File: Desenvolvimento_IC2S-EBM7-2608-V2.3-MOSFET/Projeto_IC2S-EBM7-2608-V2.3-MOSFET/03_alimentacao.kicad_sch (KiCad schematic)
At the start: 29 parts, among them T10 TP_DGND, T4 TP_+5V_REG, T5 TP_+3.3V_ANA, T6 TP_+3.3V_DIG, U14 TL431B, U3 R-78HB5.0-0.5L, U4 SPX3819M5-L-3-3/TR, U8 MCP1824ST-3302E/DB

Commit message: Revisao da reuniao 28-09: ramo unico de 24 V, 100 nF a 50 V, um so MPN de 1 uF
- Saem F2, o diodo e o condensador do ramo +24V_ADC; F1 + diodo alimentam o
  R-78HB e o +24V_ADC. +24V_REG deixa de existir (esquematico, PCB, netclasses).
- Condensador de entrada do R-78HB conferido contra o datasheet Recom (p.4):
  10 uF/100 V cumpre os 3,3 uF/100 V pedidos com Vin > 50 V. Sem alteracao.
- 100 nF fora do 24 V -> TDK C1608X7R1H104K080AA (50 V); o do +24V_ADC fica
  GRM188R72A104KA35D (100 V). 1 uF -> TDK C1608X7R1H105K080AB nos quatro.
- Notas 2, 13 e 14 da folha 2; README e registo em 00-Especificacoes;
  catalogo TDK em Documentos_de_Referencia.

Co-Authored-By: Claude Opus 5.5 (1M context) <noreply@anthropic.com>
Claude-Session: https://claude.ai/code/session_01KPnkiJQKrkjgRqqw9M78ie
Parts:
- C18, C20, C22, C23: value 100nF -> 100nF/50V; MPN GRM188R72A104KA35D -> C1608X7R1H104K080AA
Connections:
- net +24V_REG renamed +24V_ADC
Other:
- note added: "1. Cadeia analogica: +24V_ADC > U3 K78U05 > +5V_REG >"
- note removed: "1. Cadeia analogica: +24V_REG > U3 K78U05 > +5V_REG >"
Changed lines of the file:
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@@
 		)
 	)
-	(text "1. Cadeia analogica: +24V_REG > U3 K78U05 > +5V_REG >"
+	(text "1. Cadeia analogica: +24V_ADC > U3 K78U05 > +5V_REG >"
 		(exclude_from_sim no)
 		(at 35.56 102.87 0)
@@
 			)
 		)
-		(property "Value" "100nF"
+		(property "Value" "100nF/50V"
 			(at 146.05 72.39 0)
 			(show_name no)
@@
 			)
 		)
-		(property "MPN" "GRM188R72A104KA35D"
+		(property "MPN" "C1608X7R1H104K080AA"
 			(at 0 0 0)
 			(hide yes)
@@
 			)
 		)
-		(property "Value" "100nF"
+		(property "Value" "100nF/50V"
 			(at 166.37 72.39 0)
 			(show_name no)
@@
 			)
 		)
-		(property "MPN" "GRM188R72A104KA35D"
+		(property "MPN" "C1608X7R1H104K080AA"
 			(at 0 0 0)
 			(hide yes)
@@
 			)
 		)
-		(property "Value" "100nF"
+		(property "Value" "100nF/50V"
 			(at 62.738 73.914 0)
 			(show_name no)
@@
 			)
 		)
-		(property "MPN" "GRM188R72A104KA35D"
+		(property "MPN" "C1608X7R1H104K080AA"
 			(at 0 0 0)
 			(hide yes)
@@
 			)
 		)
-		(property "Value" "100nF"
+		(property "Value" "100nF/50V"
 			(at 127 147.955 0)
 			(show_name no)
@@
 			)
 		)
-		(property "MPN" "GRM188R72A104KA35D"
+		(property "MPN" "C1608X7R1H104K080AA"
 			(at 0 0 0)
 			(hide yes)
@@
 			)
 		)
-		(property "Value" "+24V_REG"
+		(property "Value" "+24V_ADC"
 			(at 30.48 58.42 0)
 			(show_name no)

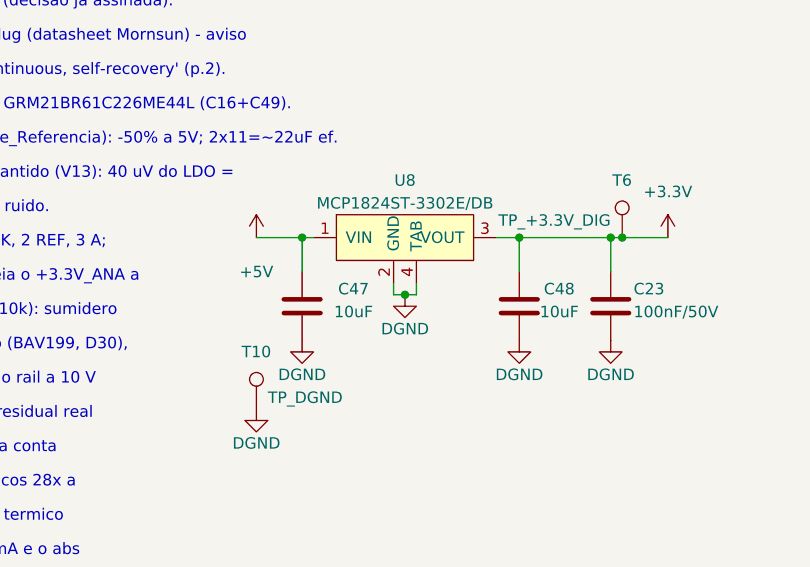
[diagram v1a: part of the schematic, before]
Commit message: LDO 3,3 V do lado PLC: U8 MCP1824ST (SOT-223) -> SPX3819M5-L-3-3/TR (SOT-23-5), mesmo MPN do U4
- Criterio da equipa: menos MPN, mais pecas do mesmo tipo; o MCP1824ST sai.
- EN a VIN, BYP aberto; estabilidade com ceramico sem garantia no datasheet (provada em campo na V2.2).
- Esquematico: ERC 0; netlist so muda os pinos do U8. PCB: pegada SOT-23-5 no
  mesmo sitio; faltam rotear 6 ligacoes do U8.
- Registo: alteracao_LDO_3V3_lado_PLC_2026-09-28.md (comparacao, verificacao e
  riscos em aberto). BOM e PDF do esquematico regenerados.

Co-Authored-By: Claude Opus 5.5 (1M context) <noreply@anthropic.com>
Claude-Session: https://claude.ai/code/session_01KPnkiJQKrkjgRqqw9M78ie
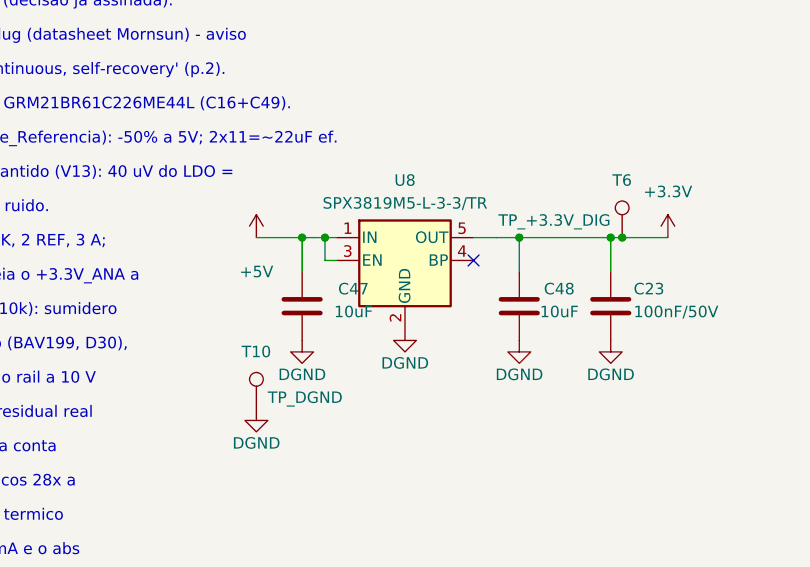
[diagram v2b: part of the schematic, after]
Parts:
- U8: value MCP1824ST-3302E/DB -> SPX3819M5-L-3-3/TR; footprint EBM7_V23:SOT-223-3 -> EBM7_V23:SOT-23-5; symbol EBM7_V23_proyecto2:MCP1824ST-3302E -> Regulator_Linear:SPX3819M5-L-3-3; MPN MCP1824ST-3302E/DB -> SPX3819M5-L-3-3/TR
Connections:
- net +3.3V: now also U8.5 (OUT); no longer U8.3 (VOUT)
- net +5V: now also U8.3 (EN)
- net DGND: no longer U8.4 (TAB)
- no-connect marks 0 -> 1
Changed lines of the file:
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@@
 	)
 	(junction
-		(at 101.6 146.05)
-		(diameter 0)
-		(color 0 0 0 0)
-	)
-	(junction
 		(at 172.72 63.5)
 		(diameter 0)
@@
 	(wire
 		(pts
-			(xy 100.33 144.78) (xy 100.33 146.05)
-		)
-		(stroke
-			(width 0)
-			(type default)
-		)
-	)
-	(wire
-		(pts
 			(xy 55.88 63.5) (xy 55.88 67.31)
 		)
@@
 	(wire
 		(pts
-			(xy 100.33 146.05) (xy 101.6 146.05)
-		)
-		(stroke
-			(width 0)
-			(type default)
-		)
-	)
-	(wire
-		(pts
 			(xy 55.88 63.5) (xy 64.77 63.5)
 		)
@@
 	(wire
 		(pts
-			(xy 102.87 146.05) (xy 102.87 144.78)
-		)
-		(stroke
-			(width 0)
-			(type default)
-		)
-	)
-	(wire
-		(pts
-			(xy 101.6 146.05) (xy 102.87 146.05)
-		)
-		(stroke
-			(width 0)
-			(type default)
-		)
-	)
-	(wire
-		(pts
 			(xy 120.65 66.04) (xy 121.92 66.04)
 		)
@@
 	(symbol
 		(lib_id "power:GND")
-		(at 101.6 146.05 0)
+		(at 101.6 149.86 0)
 		(unit 1)
 		(body_style 1)
@@
 		(dnp no)
 		(property "Reference" "#PWR0318"
-			(at 101.6 139.7 0)
+			(at 101.6 143.51 0)
 			(hide yes)
 			(show_name no)
@@
 		)
 		(property "Value" "DGND"
-			(at 101.6 149.86 0)
+			(at 101.6 153.67 0)
 			(show_name no)
 			(do_not_autoplace no)
@@
 		)
 		(property "Footprint" ""
-			(at 101.6 146.05 0)
+			(at 101.6 149.86 0)
 			(hide yes)
 			(show_name no)
@@
 		)
 		(property "Datasheet" ""
-			(at 101.6 146.05 0)
+			(at 101.6 149.86 0)
 			(hide yes)
 			(show_name no)
@@
 		)
 		(property "Description" ""
-			(at 101.6 146.05 0)
+			(at 101.6 149.86 0)
 			(show_name no)
 			(do_not_autoplace no)
@@
 	)
 	(symbol
-		(lib_id "EBM7_V23_proyecto2:MCP1824ST-3302E")
-		(at 101.6 139.7 0)
+		(lib_id "Regulator_Linear:SPX3819M5-L-3-3")
+		(at 101.6 142.24 0)
 		(unit 1)
 		(body_style 1)
@@
 			)
 		)
-		(property "Value" "MCP1824ST-3302E/DB"
+		(property "Value" "SPX3819M5-L-3-3/TR"
 			(at 101.6 135.89 0)
 			(show_name no)
@@
 			)
 		)
-		(property "Footprint" "EBM7_V23:SOT-223-3"
+		(property "Footprint" "EBM7_V23:SOT-23-5"
 			(at 101.6 139.7 0)
 			(hide yes)
@@
 			)
 		)
-		(property "MPN" "MCP1824ST-3302E/DB"
+		(property "MPN" "SPX3819M5-L-3-3/TR"
 			(at 0 0 0)
 			(hide yes)
@@
 		(pin "1"
 		)
+		(pin "2"
+		)
 		(pin "3"
 		)
 		(pin "4"
 		)
-		(pin "2"
+		(pin "5"
 		)
 		(instances
@@
 		)
 	)
+	(wire
+		(pts
+			(xy 91.44 139.7) (xy 92.71 139.7)
+		)
+		(stroke
+			(width 0)
+			(type default)
+		)
+	)
+	(wire
+		(pts
+			(xy 92.71 139.7) (xy 93.98 139.7)
+		)
+		(stroke
+			(width 0)
+			(type default)
+		)
+	)
+	(wire
+		(pts
+			(xy 93.98 142.24) (xy 92.71 142.24)
+		)
+		(stroke
+			(width 0)
+			(type default)
+		)
+	)
+	(wire
+		(pts
+			(xy 92.71 142.24) (xy 92.71 139.7)
+		)
+		(stroke
+			(width 0)
+			(type default)
+		)
+	)
+	(wire
+		(pts
+			(xy 109.22 139.7) (xy 111.76 139.7)
+		)
+		(stroke
+			(width 0)
+			(type default)
+		)
+	)
+	(junction
+		(at 92.71 139.7)
+		(diameter 0)
+		(color 0 0 0 0)
+	)
+	(no_connect
+		(at 109.22 142.24)
+	)
 	(sheet_instances

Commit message: C61 2,2 uF na saida do U8 (SPX3819), como a saida do SPX da V2.2 em campo
- Mesmo complemento da fixa (datasheet SPX3819 Fig. 18). PCB: clone do C48 a 3 mm do U8.
- ERC 0; DRC 0 erros, sem avisos novos, paridade 1 (C35, anterior).

Co-Authored-By: Claude Opus 5.5 (1M context) <noreply@anthropic.com>
Claude-Session: https://claude.ai/code/session_01KPnkiJQKrkjgRqqw9M78ie
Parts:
- added C61: 2.2uF, EBM7_V23:0603C, symbol Device:C
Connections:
- net +3.3V: now also C61.2
- net DGND: now also C61.1
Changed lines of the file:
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@@
 		(at 109.22 142.24)
+	)
+	(symbol
+		(lib_id "Device:C")
+		(at 137.16 147.32 180)
+		(unit 1)
+		(body_style 1)
+		(exclude_from_sim no)
+		(in_bom yes)
+		(on_board yes)
+		(in_pos_files yes)
+		(dnp no)
+		(property "Reference" "C61"
+			(at 141.61 145.41 0)
+			(show_name no)
+			(do_not_autoplace no)
+			(effects
+				(font
+					(size 1.27 1.27)
+				)
+			)
+		)
+		(property "Value" "2.2uF"
+			(at 141.61 147.96 0)
+			(show_name no)
+			(do_not_autoplace no)
+			(effects
+				(font
+					(size 1.27 1.27)
+				)
+			)
+		)
+		(property "Footprint" "EBM7_V23:0603C"
+			(at 137.16 147.32 180)
+			(hide yes)
+			(show_name no)
+			(do_not_autoplace no)
+			(effects
+				(font
+					(size 1.27 1.27)
+				)
+			)
+		)
+		(property "Datasheet" ""
+			(at 137.16 147.32 0)
+			(hide yes)
+			(show_name no)
+			(do_not_autoplace no)
+			(effects
+				(font
+					(size 1.27 1.27)
+				)
+			)
+		)
+		(property "Description" ""
+			(at 137.16 147.32 0)
+			(show_name no)
+			(do_not_autoplace no)
+			(effects
+				(font
+					(size 1.27 1.27)
+				)
+			)
+		)
+		(property "MPN" "C1608X5R1E225K080AB"
+			(at 22.86 0 0)
+			(hide yes)
+			(show_name no)
+			(do_not_autoplace no)
+			(effects
+				(font
+					(size 1.27 1.27)
+				)
+			)
+		)
+		(pin "1"
+		)
+		(pin "2"
+		)
+		(instances
+			(project "IC2S-EBM7-2608-V2.3-MOSFET"
+				(path "/ea39faa7-2c85-4731-99b5-dc619370fd78/82f69a70-41b2-4a25-bf1f-10081957b908"
+					(reference "C61")
+					(unit 1)
+				)
+			)
+		)
+	)
+	(symbol
+		(lib_id "power:GND")
+		(at 137.16 151.13 0)
+		(unit 1)
+		(body_style 1)
+		(exclude_from_sim no)
+		(in_bom yes)
+		(on_board yes)
+		(in_pos_files yes)
+		(dnp no)
+		(property "Reference" "#PWR0802"
+			(at 137.16 144.78 0)
+			(hide yes)
+			(show_name no)
+			(do_not_autoplace no)
+			(effects
+				(font
+					(size 1.27 1.27)
+				)
+			)
+		)
+		(property "Value" "DGND"
+			(at 137.16 154.94 0)
+			(show_name no)
+			(do_not_autoplace no)
+			(effects
+				(font
+					(size 1.27 1.27)
+				)
+			)
+		)
+		(property "Footprint" ""
+			(at 137.16 151.13 0)
+			(hide yes)
+			(show_name no)
+			(do_not_autoplace no)
+			(effects
+				(font
+					(size 1.27 1.27)
+				)
+			)
+		)
+		(property "Datasheet" ""
+			(at 137.16 151.13 0)
+			(hide yes)
+			(show_name no)
+			(do_not_autoplace no)
+			(effects
+				(font
+					(size 1.27 1.27)
+				)
+			)
+		)
+		(property "Description" ""
+			(at 137.16 151.13 0)
+			(show_name no)
+			(do_not_autoplace no)
+			(effects
+				(font
+					(size 1.27 1.27)
+				)
+			)
+		)
+		(pin "1"
+		)
+		(instances
+			(project "IC2S-EBM7-2608-V2.3-MOSFET"
+				(path "/ea39faa7-2c85-4731-99b5-dc619370fd78/82f69a70-41b2-4a25-bf1f-10081957b908"
+					(reference "#PWR0802")
+					(unit 1)
+				)
+			)
+		)
+	)
+	(symbol
+		(lib_id "power:+3V3")
+		(at 137.16 143.51 0)
+		(unit 1)
+		(body_style 1)
+		(exclude_from_sim no)
+		(in_bom yes)
+		(on_board yes)
+		(in_pos_files yes)
+		(dnp no)
+		(property "Reference" "#PWR0803"
+			(at 137.16 137.16 0)
+			(hide yes)
+			(show_name no)
+			(do_not_autoplace no)
+			(effects
+				(font
+					(size 1.27 1.27)
+				)
+			)
+		)
+		(property "Value" "+3.3V"
+			(at 137.16 138.43 0)
+			(show_name no)
+			(do_not_autoplace no)
+			(effects
+				(font
+					(size 1.27 1.27)
+				)
+			)
+		)
+		(property "Footprint" ""
+			(at 137.16 143.51 0)
+			(hide yes)
+			(show_name no)
+			(do_not_autoplace no)
+			(effects
+				(font
+					(size 1.27 1.27)
+				)
+			)
+		)
+		(property "Datasheet" ""
+			(at 137.16 143.51 0)
+			(hide yes)
+			(show_name no)
+			(do_not_autoplace no)
+			(effects
+				(font
+					(size 1.27 1.27)
+				)
+			)
+		)
+		(property "Description" ""
+			(at 137.16 143.51 0)
+			(show_name no)
+			(do_not_autoplace no)
+			(effects
+				(font
+					(size 1.27 1.27)
+				)
+			)
+		)
+		(pin "1"
+		)
+		(instances
+			(project "IC2S-EBM7-2608-V2.3-MOSFET"
+				(path "/ea39faa7-2c85-4731-99b5-dc619370fd78/82f69a70-41b2-4a25-bf1f-10081957b908"
+					(reference "#PWR0803")
+					(unit 1)
+				)
+			)
+		)
 	)
 	(sheet_instances
